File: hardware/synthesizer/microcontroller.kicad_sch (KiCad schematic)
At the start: 43 parts, among them U2 LAN8742A, U4 STM32H723VGTx, Y1 48MHz/8pF

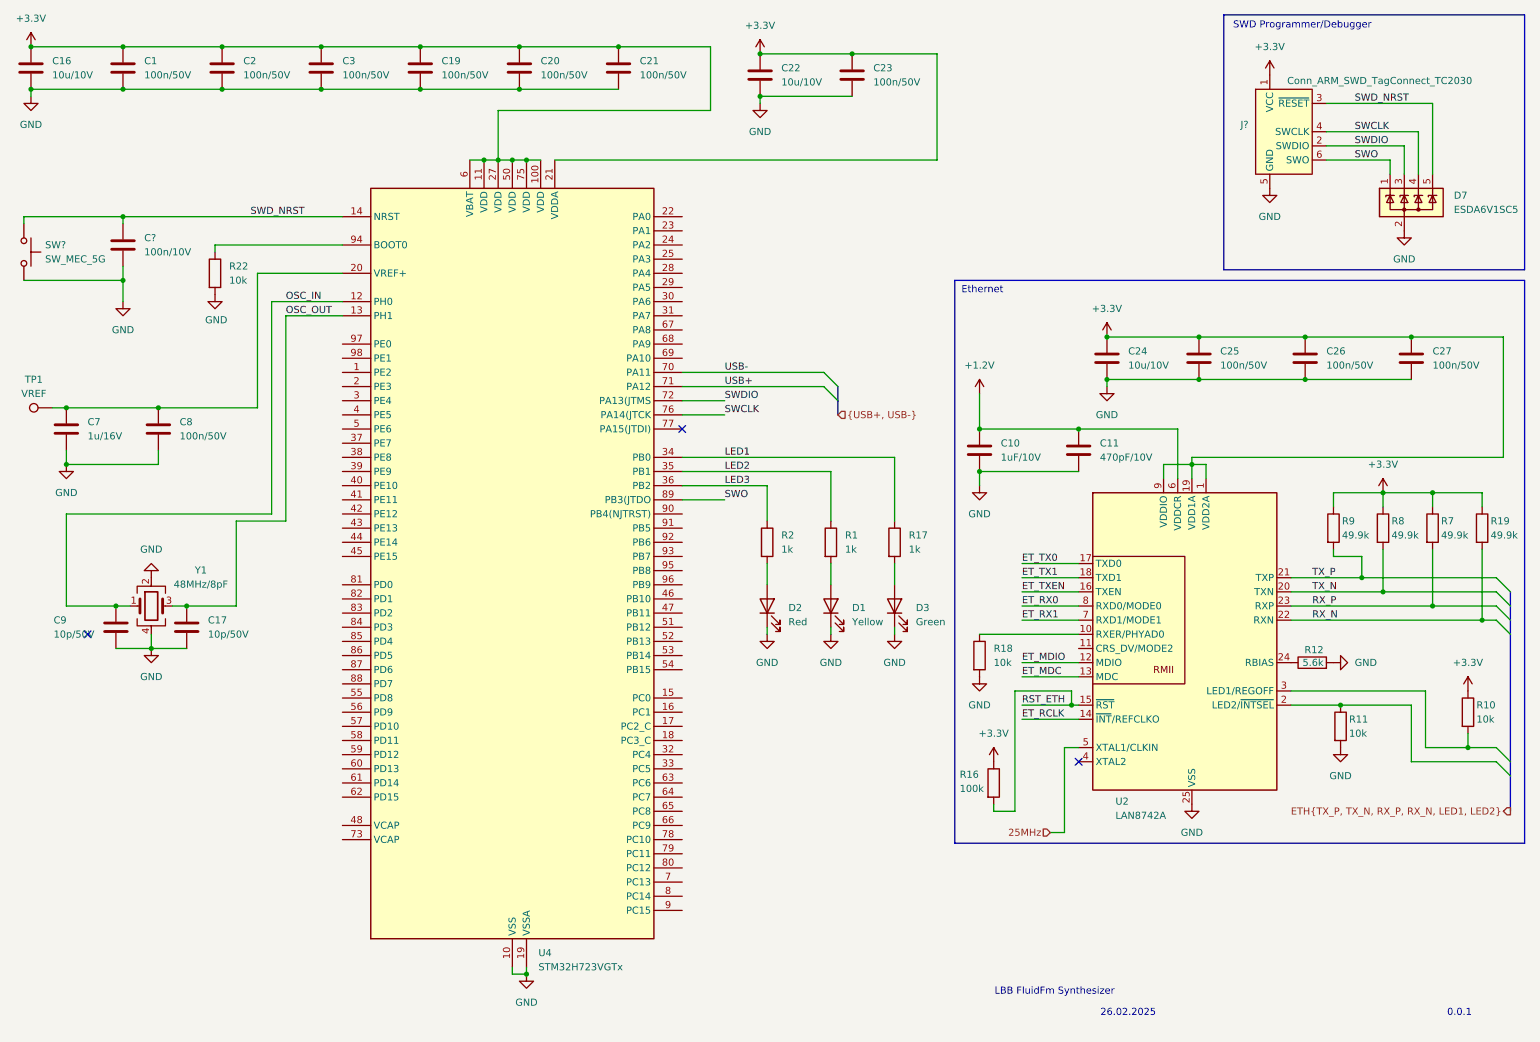
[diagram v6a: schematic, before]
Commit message: work on synthesizer schematics - add HSE and LSE oscillators
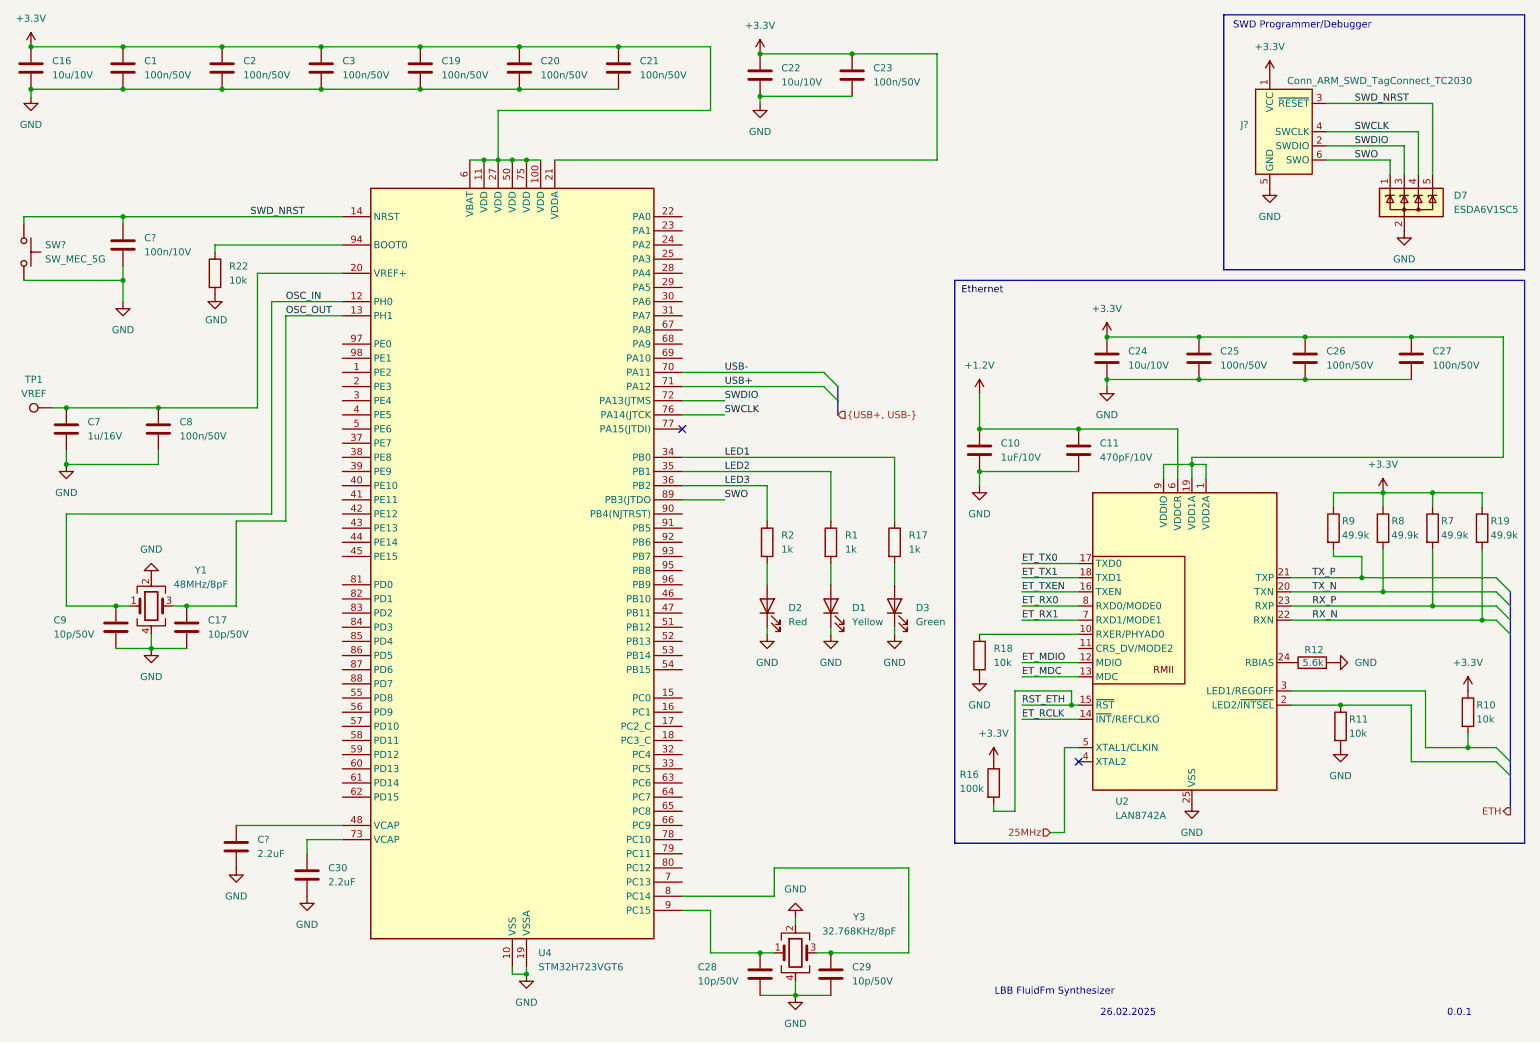
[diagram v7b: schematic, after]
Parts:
- added C28, C29: 10p/50V, symbol Device:C
- added C30, C?: 2.2uF, symbol Device:C
- added Y3: 32.768KHz/8pF, symbol Device:Crystal_GND24
- U4: value STM32H723VGTx -> STM32H723VGT6
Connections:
- net GND: now also C28.2, C29.2, C30.2, C?.2, Y3.2, Y3.4
- net at U4.48 (VCAP): now also C?.1
- net at U4.73 (VCAP): now also C30.1
- net at U4.8 (PC14): now also C29.1, Y3.3
- net at U4.9 (PC15): now also C28.1, Y3.1
- no-connect marks 3 -> 2

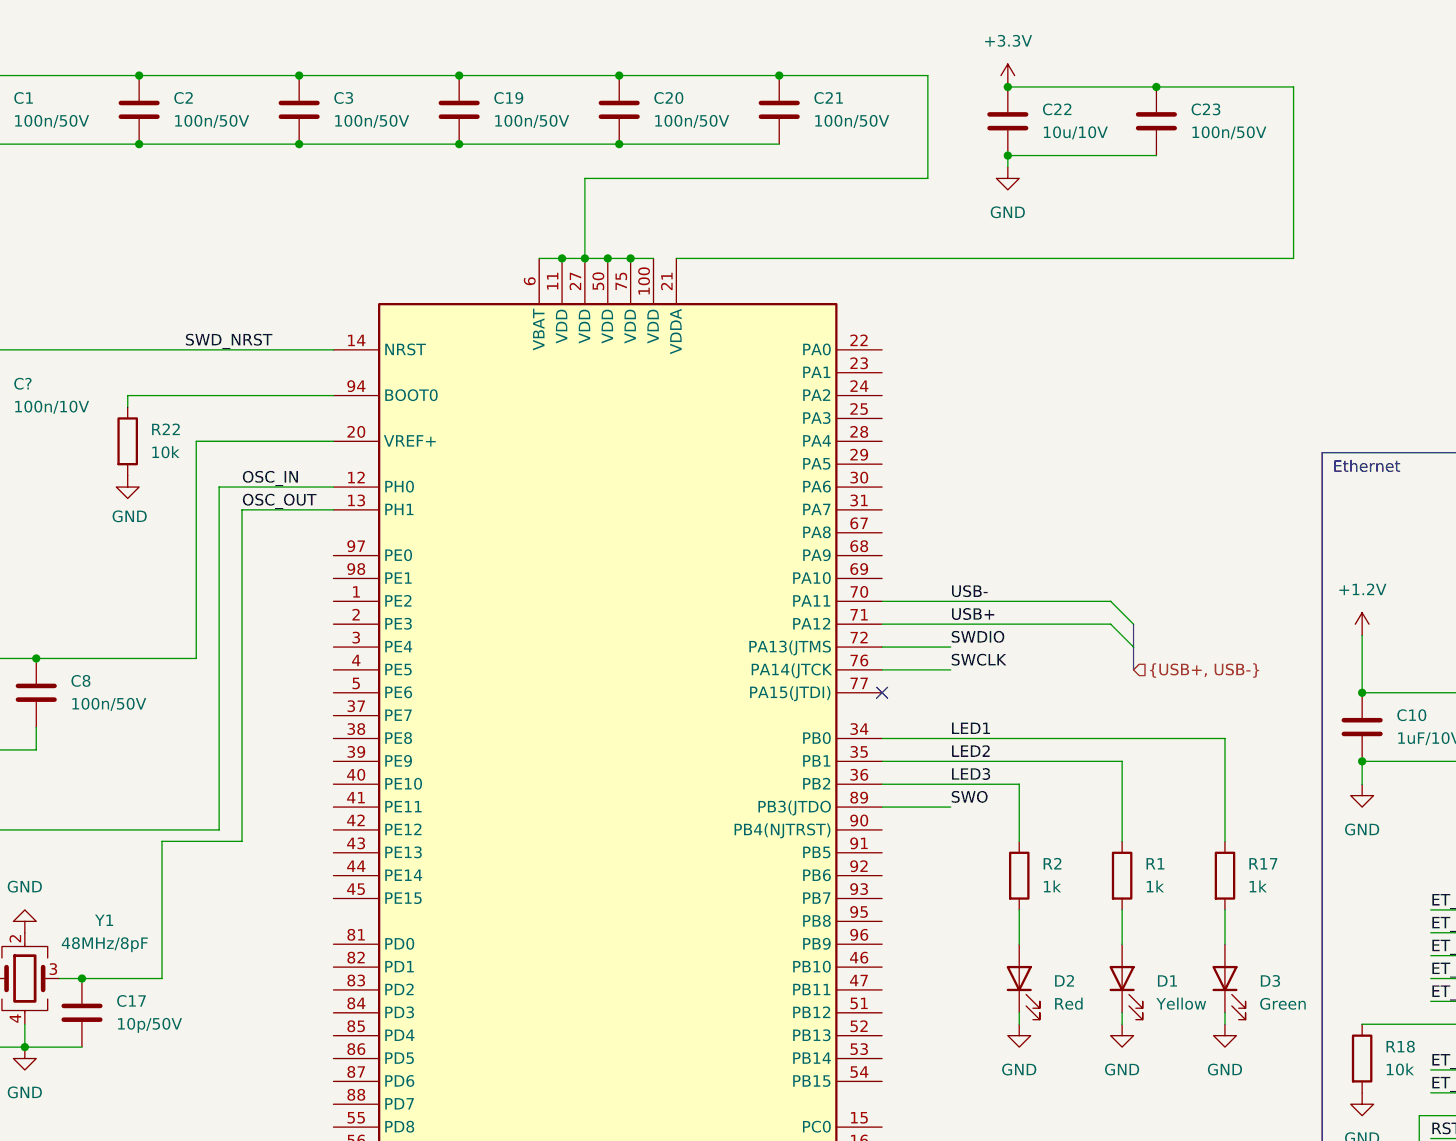
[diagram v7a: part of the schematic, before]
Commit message: add dac test
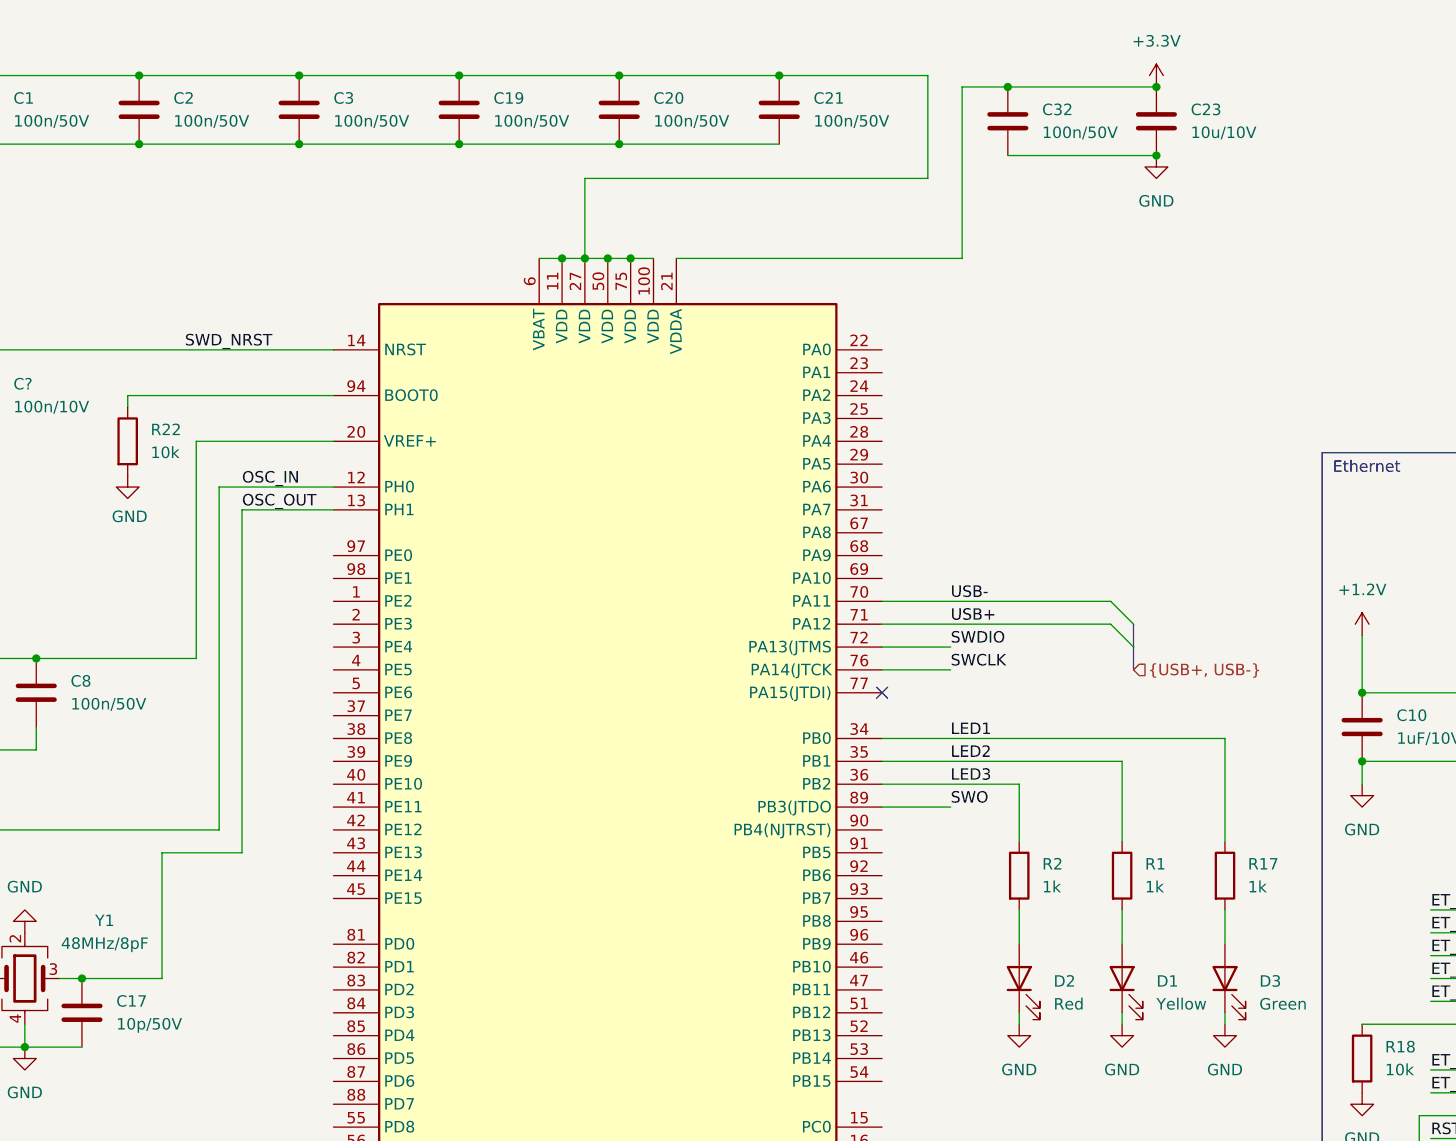
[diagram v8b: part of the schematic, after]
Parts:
- removed C22: 10u/10V, symbol Device:C
- added C32: 100n/50V, symbol Device:C
- C23: value 100n/50V -> 10u/10V
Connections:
- net +3.3V: now also C32.1
- net GND: now also C32.2
